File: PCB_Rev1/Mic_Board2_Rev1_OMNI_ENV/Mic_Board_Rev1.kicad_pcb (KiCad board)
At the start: 2 copper layers, 26 parts, among them J1 Conn_01x03_Pin, J2 532610771, U1 OPA1671IDBVR

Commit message: Micboard pcb
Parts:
- moved MK1 40.5 mm to (145.5, 70.0)
- moved J2 32.7 mm to (75.0, 73.0), turned to 90 degrees
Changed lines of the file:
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@@
 	(footprint "Footprints:Omnidirectional"
 		(layer "F.Cu")
-		(at 105.02695 68.070799)
+		(at 145.5 70)
 		(property "Reference" "MK1"
 			(at -0.635215 -5.717015 0)
@@
 	(footprint "Footprints:HeaderConnection"
 		(layer "F.Cu")
-		(at 103.22705 56.501499)
+		(at 75 73 90)
 		(tags "532610771 ")
 		(property "Reference" "J2"
-			(at 0 2.9045 0)
+			(at 0 2.9045 90)
 			(unlocked yes)
 			(layer "F.SilkS")
@@
 		)
 		(property "Value" "532610771"
-			(at 0 2.9045 0)
+			(at 0 2.9045 90)
 			(unlocked yes)
 			(layer "F.Fab")
@@
 		)
 		(property "Footprint" "Footprints:HeaderConnection"
-			(at 0 0 0)
+			(at 0 0 90)
 			(layer "F.Fab")
 			(hide yes)
@@
 		)
 		(property "Datasheet" ""
-			(at 0 0 0)
+			(at 0 0 90)
 			(layer "F.Fab")
 			(hide yes)
@@
 		)
 		(property "Description" "\nPicoblade Connector, 7 Circuit Single Row, Right Angle Surface Mount SMT PCB\n"
-			(at 0 0 0)
+			(at 0 0 90)
 			(layer "F.Fab")
 			(hide yes)
@@
 		)
 		(property "DigiKey_Part_Number" "WM7625TR-ND"
-			(at 0 0 0)
+			(at 0 0 90)
 			(unlocked yes)
 			(layer "F.Fab")
@@
 		)
 		(property "MF" "Molex"
-			(at 0 0 0)
+			(at 0 0 90)
 			(unlocked yes)
 			(layer "F.Fab")
@@
 		)
 		(property "MAXIMUM_PACKAGE_HEIGHT" "3.4 mm"
-			(at 0 0 0)
+			(at 0 0 90)
 			(unlocked yes)
 			(layer "F.Fab")
@@
 		)
 		(property "Package" "None"
-			(at 0 0 0)
+			(at 0 0 90)
 			(unlocked yes)
 			(layer "F.Fab")
@@
 		)
 		(property "Check_prices" "https://www.snapeda.com/parts/0532610771/Molex/view-part/?ref=eda"
-			(at 0 0 0)
+			(at 0 0 90)
 			(unlocked yes)
 			(layer "F.Fab")
@@
 		)
 		(property "STANDARD" "Manufacturer Recommendations"
-			(at 0 0 0)
+			(at 0 0 90)
 			(unlocked yes)
 			(layer "F.Fab")
@@
 		)
 		(property "PARTREV" "J"
-			(at 0 0 0)
+			(at 0 0 90)
 			(unlocked yes)
 			(layer "F.Fab")
@@
 		)
 		(property "SnapEDA_Link" "https://www.snapeda.com/parts/0532610771/Molex/view-part/?ref=snap"
-			(at 0 0 0)
+			(at 0 0 90)
 			(unlocked yes)
 			(layer "F.Fab")
@@
 		)
 		(property "MP" "0532610771"
-			(at 0 0 0)
+			(at 0 0 90)
 			(unlocked yes)
 			(layer "F.Fab")
@@
 		)
 		(property "Purchase-URL" "https://www.snapeda.com/api/url_track_click_mouser/?unipart_id=577144&manufacturer=Molex&part_name=0532610771&search_term=None"
-			(at 0 0 0)
+			(at 0 0 90)
 			(unlocked yes)
 			(layer "F.Fab")
@@
 		)
 		(property "MANUFACTURER" "Molex"
-			(at 0 0 0)
+			(at 0 0 90)
 			(unlocked yes)
 			(layer "F.Fab")
@@
 		)
 		(fp_line
-			(start -6.8834 -2.2225)
-			(end -6.8834 -1.877639)
+			(start 6.8834 -2.2225)
+			(end -6.8834 -2.2225)
 			(stroke
 				(width 0.1524)
@@
 		)
 		(fp_line
-			(start -6.8834 1.886641)
-			(end -6.8834 2.2225)
+			(start -6.8834 -2.2225)
+			(end -6.8834 -1.877639)
 			(stroke
 				(width 0.1524)
@@
 		)
 		(fp_line
-			(start -6.8834 2.2225)
-			(end -4.48914 2.2225)
+			(start 6.8834 -1.877639)
+			(end 6.8834 -2.2225)
 			(stroke
 				(width 0.1524)
@@
 		)
 		(fp_line
-			(start 4.48914 2.2225)
-			(end 6.8834 2.2225)
+			(start -6.8834 1.886641)
+			(end -6.8834 2.2225)
 			(stroke
 				(width 0.1524)
@@
 		)
 		(fp_line
-			(start 6.8834 -2.2225)
-			(end -6.8834 -2.2225)
+			(start 6.8834 2.2225)
+			(end 6.8834 1.886641)
 			(stroke
 				(width 0.1524)
@@
 		)
 		(fp_line
-			(start 6.8834 -1.877639)
-			(end 6.8834 -2.2225)
+			(start 4.48914 2.2225)
+			(end 6.8834 2.2225)
 			(stroke
 				(width 0.1524)
@@
 		)
 		(fp_line
-			(start 6.8834 2.2225)
-			(end 6.8834 1.886641)
+			(start -6.8834 2.2225)
+			(end -4.48914 2.2225)
 			(stroke
 				(width 0.1524)
@@
 		)
 		(fp_line
-			(start -7.6589 -2.3495)
-			(end -7.6589 4.0094)
+			(start 7.6589 -2.3495)
+			(end -7.6589 -2.3495)
 			(stroke
 				(width 0.1524)
@@
 		)
 		(fp_line
-			(start -7.6589 4.0094)
-			(end 7.6589 4.0094)
+			(start -7.6589 -2.3495)
+			(end -7.6589 4.0094)
 			(stroke
 				(width 0.1524)
@@
 		)
 		(fp_line
-			(start 7.6589 -2.3495)
-			(end -7.6589 -2.3495)
+			(start 7.6589 4.0094)
+			(end 7.6589 -2.3495)
 			(stroke
 				(width 0.1524)
@@
 		)
 		(fp_line
-			(start 7.6589 4.0094)
-			(end 7.6589 -2.3495)
+			(start -7.6589 4.0094)
+			(end 7.6589 4.0094)
 			(stroke
 				(width 0.1524)
@@
 		)
 		(fp_line
-			(start -6.7564 -2.0955)
-			(end -6.7564 2.0955)
+			(start 6.7564 -2.0955)
+			(end -6.7564 -2.0955)
 			(stroke
 				(width 0.0254)
@@
 		)
 		(fp_line
-			(start -6.7564 2.0955)
-			(end 6.7564 2.0955)
+			(start -6.7564 -2.0955)
+			(end -6.7564 2.0955)
 			(stroke
 				(width 0.0254)
@@
 		)
 		(fp_line
-			(start 6.7564 -2.0955)
-			(end -6.7564 -2.0955)
+			(start 6.7564 2.0955)
+			(end 6.7564 -2.0955)
 			(stroke
 				(width 0.0254)
@@
 		)
 		(fp_line
-			(start 6.7564 2.0955)
-			(end 6.7564 -2.0955)
+			(start -6.7564 2.0955)
+			(end 6.7564 2.0955)
 			(stroke
 				(width 0.0254)
@@
 		)
 		(fp_text user "${REFERENCE}"
-			(at 0 2.9045 0)
+			(at 0 2.9045 90)
 			(unlocked yes)
 			(layer "F.Fab")
@@
 		)
 		(pad "1" smd rect
-			(at 3.75 2.9045)
+			(at 3.75 2.9045 90)
 			(size 0.8128 1.7018)
 			(layers "F.Cu" "F.Paste" "F.Mask")
@@
 		)
 		(pad "2" smd rect
-			(at 2.5 2.9045)
+			(at 2.5 2.9045 90)
 			(size 0.8128 1.7018)
 			(layers "F.Cu" "F.Paste" "F.Mask")
@@
 		)
 		(pad "3" smd rect
-			(at 1.25 2.9045)
+			(at 1.25 2.9045 90)
 			(size 0.8128 1.7018)
 			(layers "F.Cu" "F.Paste" "F.Mask")
@@
 		)
 		(pad "4" smd rect
-			(at 0 2.9045)
+			(at 0 2.9045 90)
 			(size 0.8128 1.7018)
 			(layers "F.Cu" "F.Paste" "F.Mask")
@@
 		)
 		(pad "5" smd rect
-			(at -1.25 2.9045)
+			(at -1.25 2.9045 90)
 			(size 0.8128 1.7018)
 			(layers "F.Cu" "F.Paste" "F.Mask")
@@
 		)
 		(pad "6" smd rect
-			(at -2.5 2.9045)
+			(at -2.5 2.9045 90)
 			(size 0.8128 1.7018)
 			(layers "F.Cu" "F.Paste" "F.Mask")
@@
 		)
 		(pad "7" smd rect
-			(at -3.75 2.9045)
+			(at -3.75 2.9045 90)
 			(size 0.8128 1.7018)
 			(layers "F.Cu" "F.Paste" "F.Mask")
@@
 		)
 		(pad "8" smd rect
-			(at -6.3 0.004501)
+			(at -6.3 0.004501 90)
 			(size 2.2098 3.0988)
 			(layers "F.Cu" "F.Paste" "F.Mask")
 		)
 		(pad "9" smd rect
-			(at 6.3 0.004501)
+			(at 6.3 0.004501 90)
 			(size 2.2098 3.0988)
 			(layers "F.Cu" "F.Paste" "F.Mask")

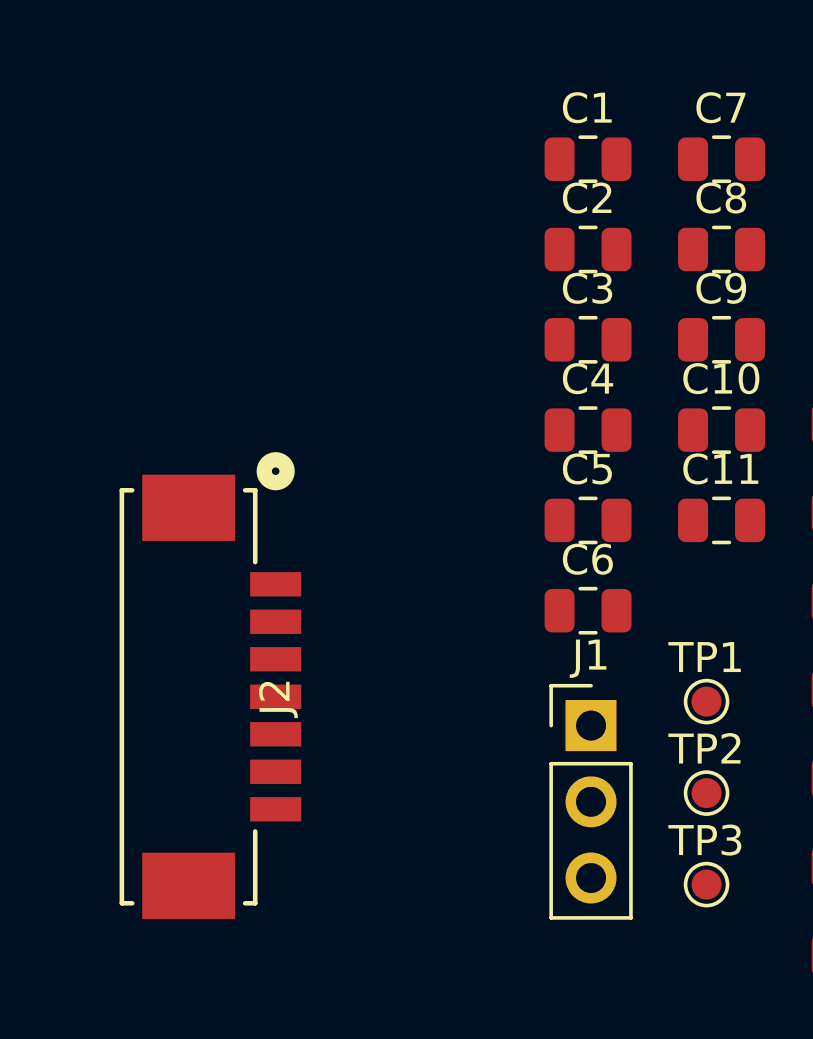
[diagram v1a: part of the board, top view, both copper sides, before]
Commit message: connections for gpio and micboards
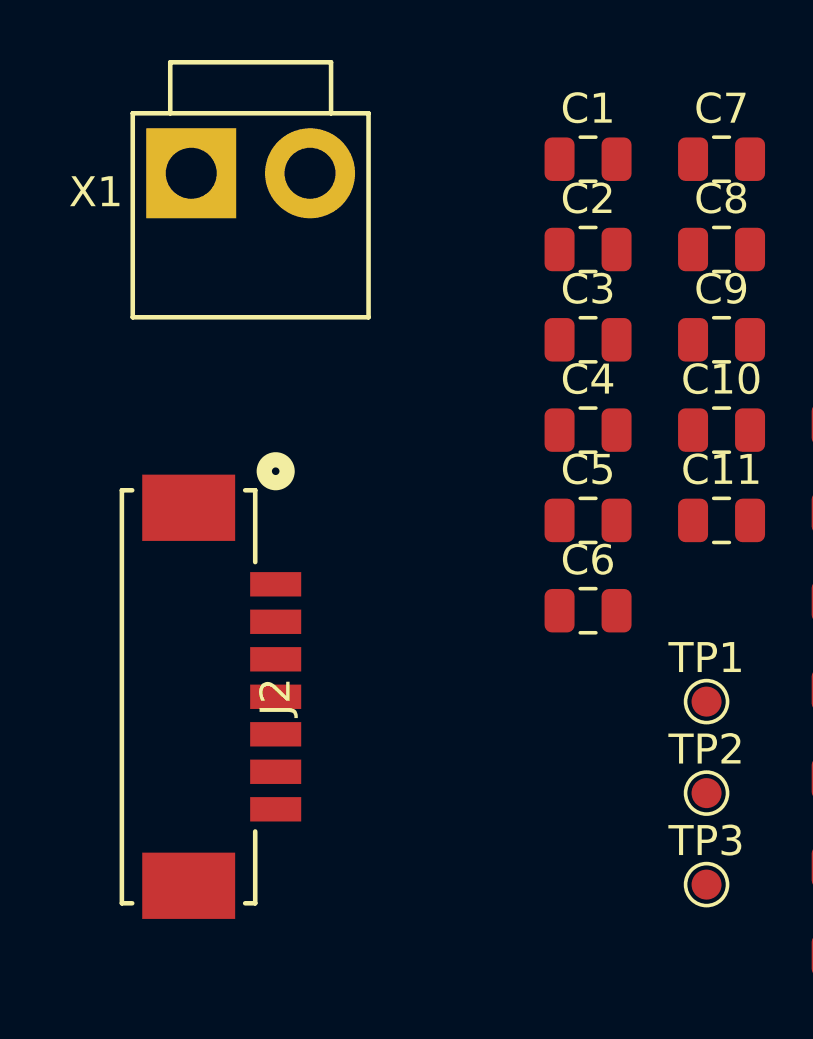
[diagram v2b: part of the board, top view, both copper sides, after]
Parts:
- removed J1: Conn_01x03_Pin, Connector_PinHeader_2.54mm:PinHeader_1x03_P2.54mm_Vertical
- added X1: B2P-VH, Footprints:B2P-VH, F.Cu at (77.1, 55.5)
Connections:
- J2 pad 5: +3V3 -> Net-(U2-FSEL)
- J2 pad 6: GND -> +3V3
- J2 pad 7: unconnected-(J2-Pad7) -> GND
- U2 pad 13: Net-(J1-Pin_1) -> GND
- U2 pad 15: Net-(J1-Pin_3) -> Net-(U2-FSEL)
